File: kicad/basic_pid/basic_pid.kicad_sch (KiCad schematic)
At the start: 72 parts, among them J1 Input A, J2 Input B / Setpoint, J3 Monitor, J4 Output, SW1 SW_DPDT_x2, SW2 SW_DPDT_x2, SW3 SW_DPDT_x2, SW4 SW_SP4T, SW5 SW_DPDT_x2, SW6 SW_SP4T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

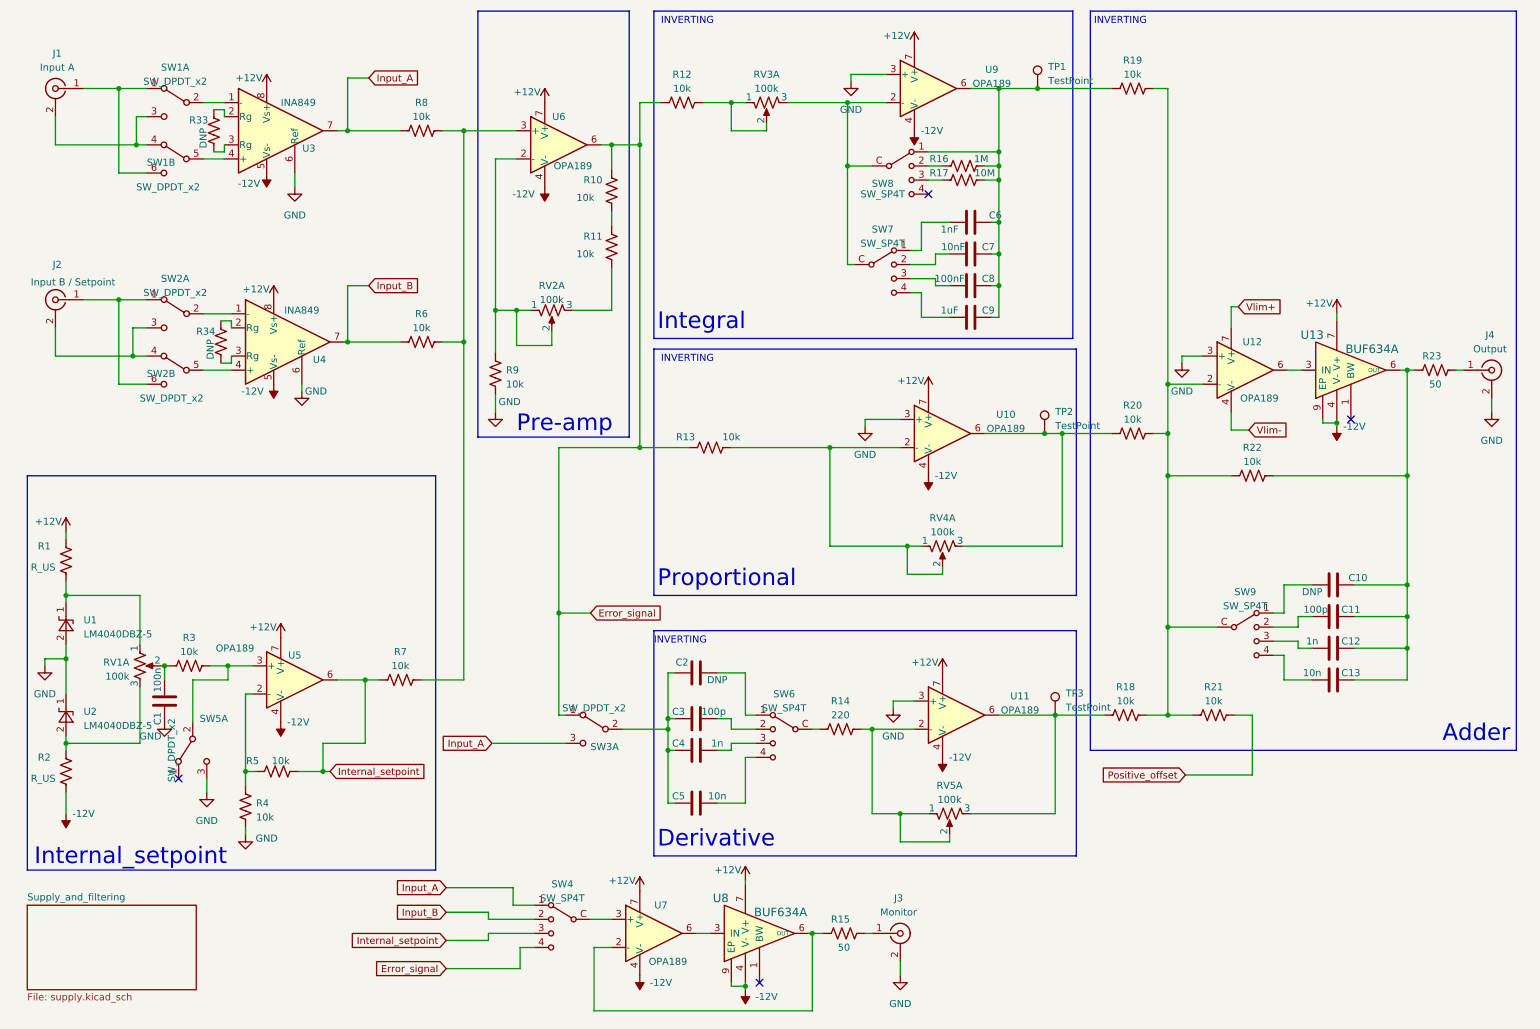
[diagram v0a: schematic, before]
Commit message: Fixed wrong part and added shunt resistor values
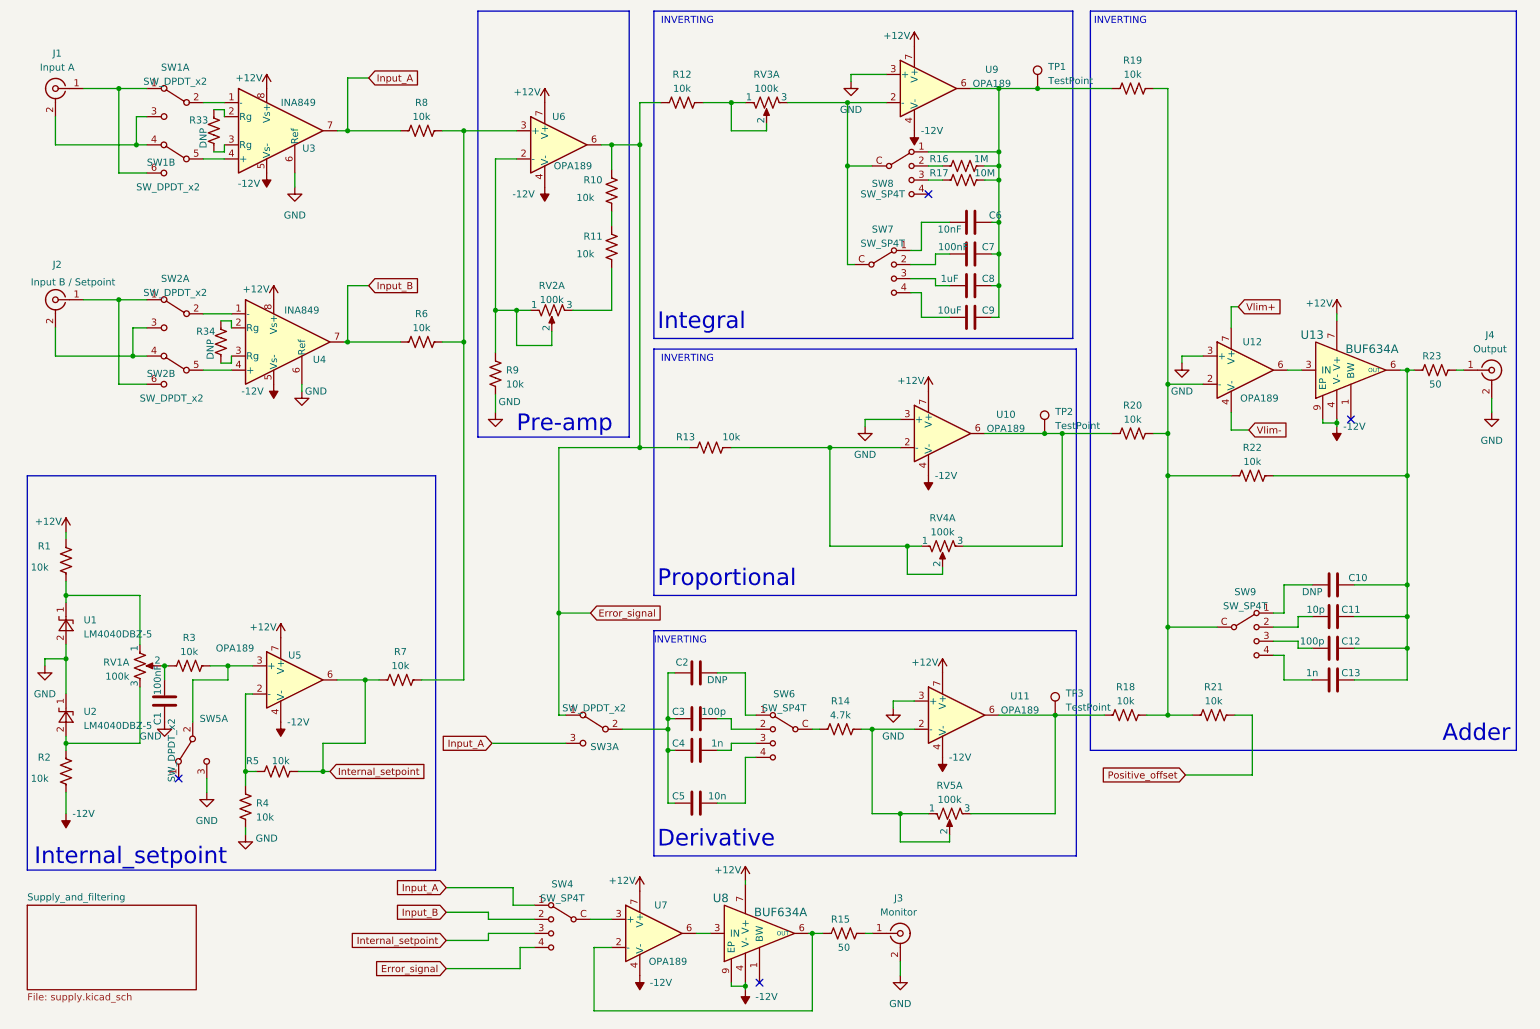
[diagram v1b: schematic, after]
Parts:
- C1: value 100n -> 100nF
- C11: value 100p -> 10p
- C12: value 1n -> 100p
- C13: value 10n -> 1n
- C6: value 1nF -> 10nF
- C7: value 10nF -> 100nF
- C8: value 100nF -> 1uF
- C9: value 1uF -> 10uF
- R1, R2: value R_US -> 10k
- R14: value 220 -> 4.7k
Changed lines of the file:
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@@
       (effects (font (size 1.27 1.27)))
     )
-    (property "Value" "220" (at 160.655 142.24 90)
+    (property "Value" "4.7k" (at 160.655 142.24 90)
       (effects (font (size 1.27 1.27)))
     )
@@
       (effects (font (size 1.27 1.27)))
     )
-    (property "Value" "100p" (at 246.38 123.19 90)
+    (property "Value" "10p" (at 246.38 123.19 90)
       (effects (font (size 1.27 1.27)))
     )
@@
       (effects (font (size 1.27 1.27)) (justify right))
     )
-    (property "Value" "R_US" (at 14.605 153.67 0)
+    (property "Value" "10k" (at 14.605 153.67 0)
       (effects (font (size 1.27 1.27)) (justify right))
     )
@@
       (effects (font (size 1.27 1.27)))
     )
-    (property "Value" "100n" (at 37.465 135.89 90)
+    (property "Value" "100nF" (at 37.465 135.89 90)
       (effects (font (size 1.27 1.27)))
     )
@@
       (effects (font (size 1.27 1.27)))
     )
-    (property "Value" "10n" (at 245.745 134.62 90)
+    (property "Value" "1n" (at 245.745 134.62 90)
       (effects (font (size 1.27 1.27)))
     )
@@
       (effects (font (size 1.27 1.27)) (justify right))
     )
-    (property "Value" "R_US" (at 14.605 115.57 0)
+    (property "Value" "10k" (at 14.605 115.57 0)
       (effects (font (size 1.27 1.27)) (justify right))
     )
@@
       (effects (font (size 1.27 1.27)))
     )
-    (property "Value" "1uF" (at 180.34 69.215 90)
+    (property "Value" "10uF" (at 180.34 69.215 90)
       (effects (font (size 1.27 1.27)))
     )
@@
       (effects (font (size 1.27 1.27)))
     )
-    (property "Value" "1n" (at 245.745 128.905 90)
+    (property "Value" "100p" (at 245.745 128.905 90)
       (effects (font (size 1.27 1.27)))
     )
@@
       (effects (font (size 1.27 1.27)))
     )
-    (property "Value" "10nF" (at 180.975 57.785 90)
+    (property "Value" "100nF" (at 180.975 57.785 90)
       (effects (font (size 1.27 1.27)))
     )
@@
       (effects (font (size 1.27 1.27)))
     )
-    (property "Value" "1nF" (at 180.34 54.61 90)
+    (property "Value" "10nF" (at 180.34 54.61 90)
       (effects (font (size 1.27 1.27)))
     )
@@
       (effects (font (size 1.27 1.27)))
     )
-    (property "Value" "100nF" (at 180.34 63.5 90)
-      (effects (font (size 1.27 1.27)))
-    )
+    (property "Value" "1uF" (at 180.34 63.5 90)
+      (effects (font (size 1.27 1.27)))
+    )

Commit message: Fixed monitor instability
Added a 3.3 kOhm resistor on each output buffer's bandwith control pin
to increase the bandwidth from 30 MHz to 90 MHz.
This should prevent oscillations and instabilities we noticed while
testing the PID
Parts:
- added R35, R36: 3.3k, Resistor_SMD:R_0805_2012Metric, symbol Device:R_US
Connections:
- net -12V: now also R35.1, R36.1
- net at U8.1 (BW): now also R36.2
- net at U13.1 (BW): now also R35.2
- no-connect marks 4 -> 2
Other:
- moved on the sheet: J3, R15, R22

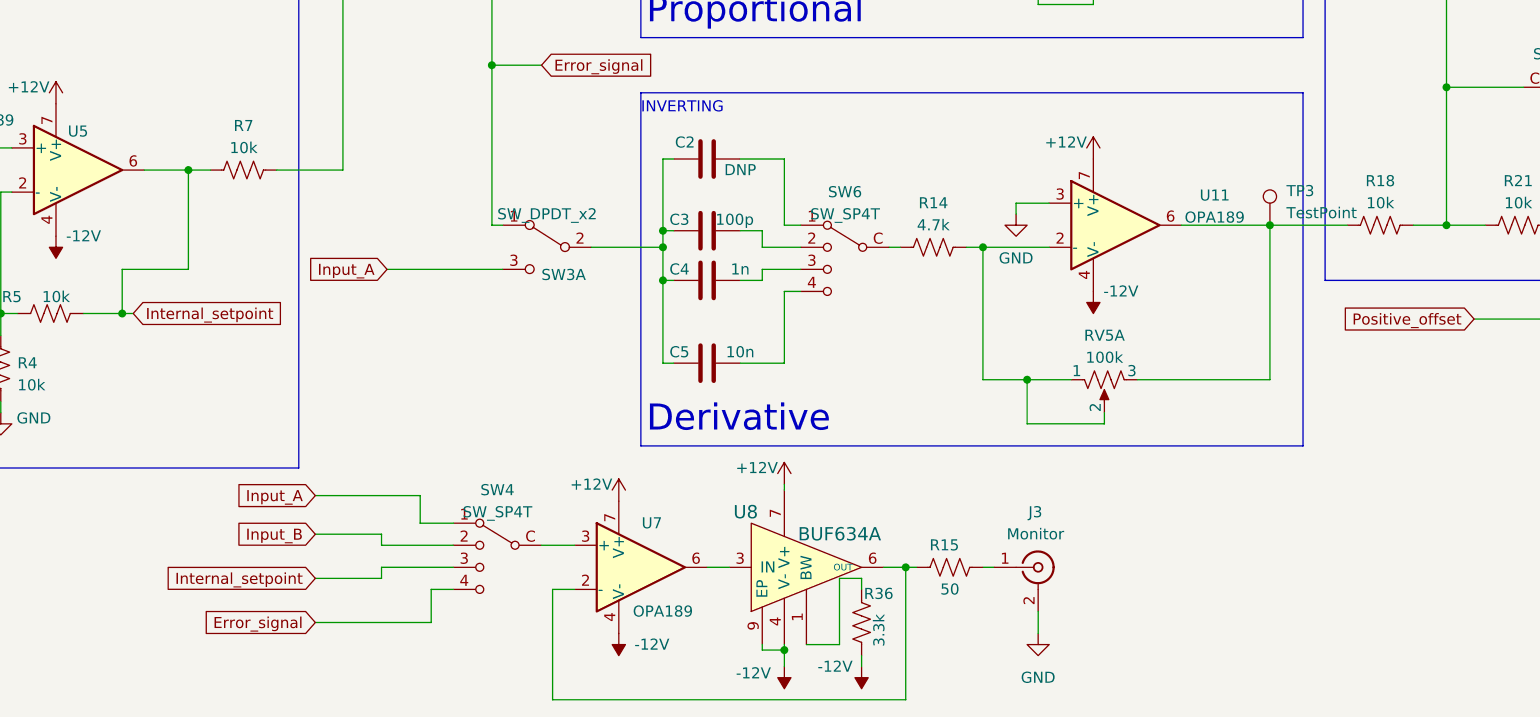
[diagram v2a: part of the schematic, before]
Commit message: Not sure if it works: Just a possibile fix for a noisy monitor when sampling error signal
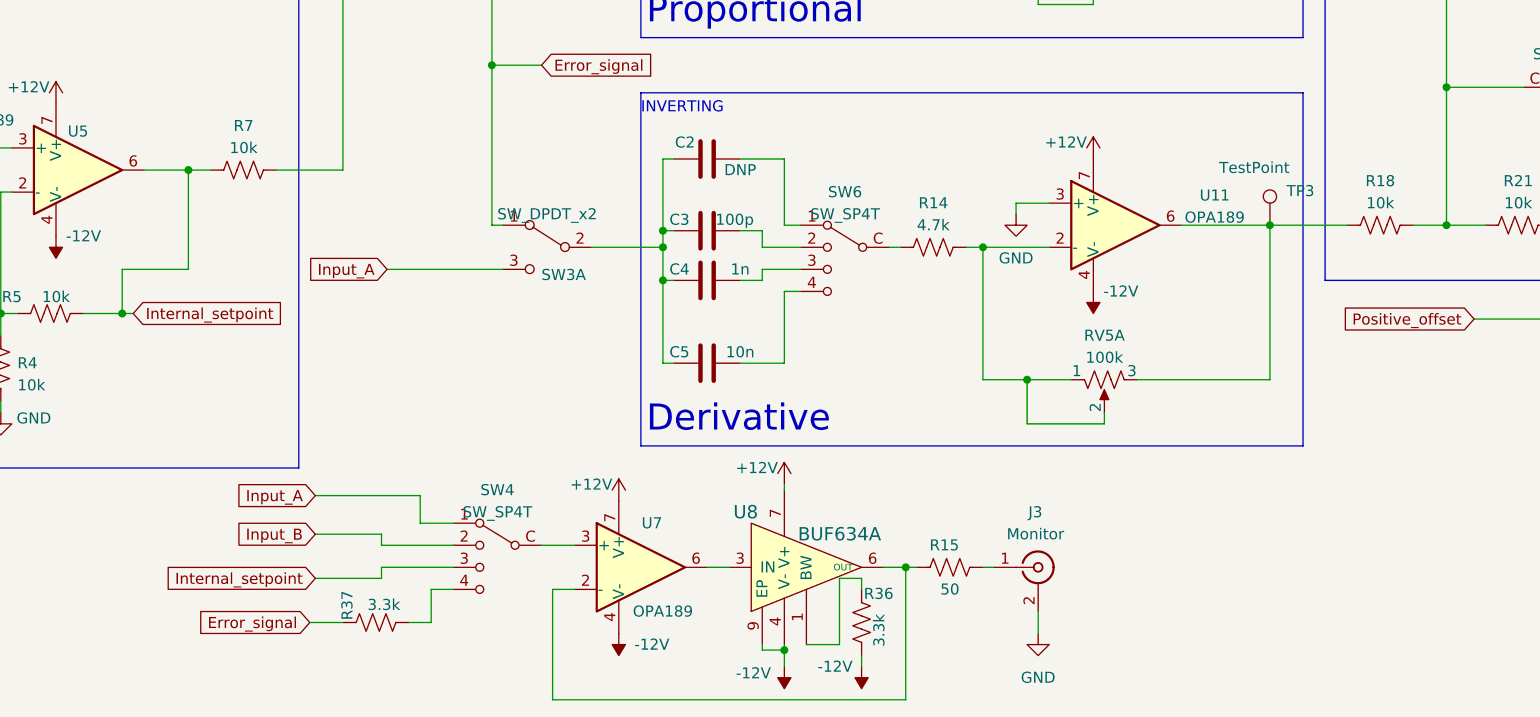
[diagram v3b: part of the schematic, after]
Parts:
- added R37: 3.3k, Resistor_SMD:R_0805_2012Metric, symbol Device:R_US
- R16: MPN (none) -> AC0805JR-071ML
- R17: MPN (none) -> RC0805JR-0710ML
- RV1, RV2, RV3, RV4, RV5: MPN (none) -> PTL45-15O0-104B1
- SW1, SW2, SW3, SW5: MPN (none) -> 1825289-1
- SW4, SW6, SW7, SW8, SW9: MPN (none) -> SLB1470
- U1, U2: MPN (none) -> LM4040B50FTA
- U10, U11, U12, U5, U6, U7, U9: MPN (none) -> OPA189ID
- U13, U8: MPN (none) -> BUF634AIDDAR
- U3, U4: MPN (none) -> INA849DR‎
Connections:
- net Error_signal: now also R37.2; no longer SW4.4
- new net: R37.1, SW4.4
